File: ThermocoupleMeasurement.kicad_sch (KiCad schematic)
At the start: 11 parts, among them U10 MAX4238ASA, U15 LT1025CN8-PBF, U9 LT1054

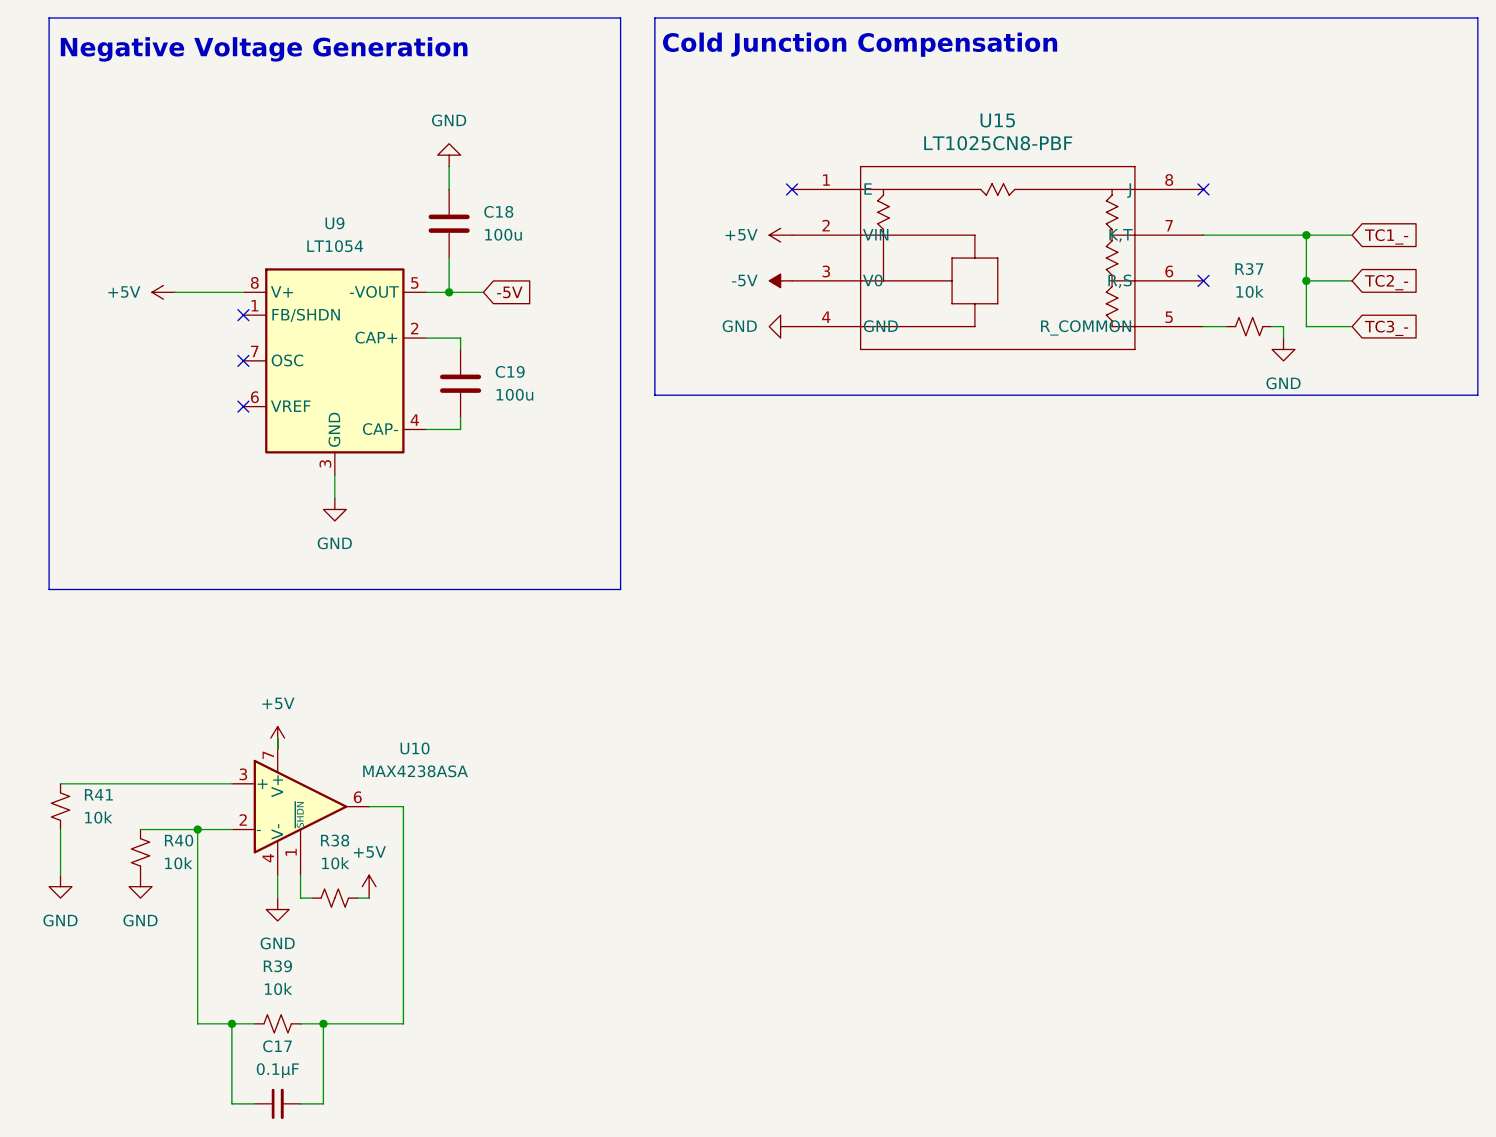
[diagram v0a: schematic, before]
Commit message: add thermocouple filtering, add 5th ADC
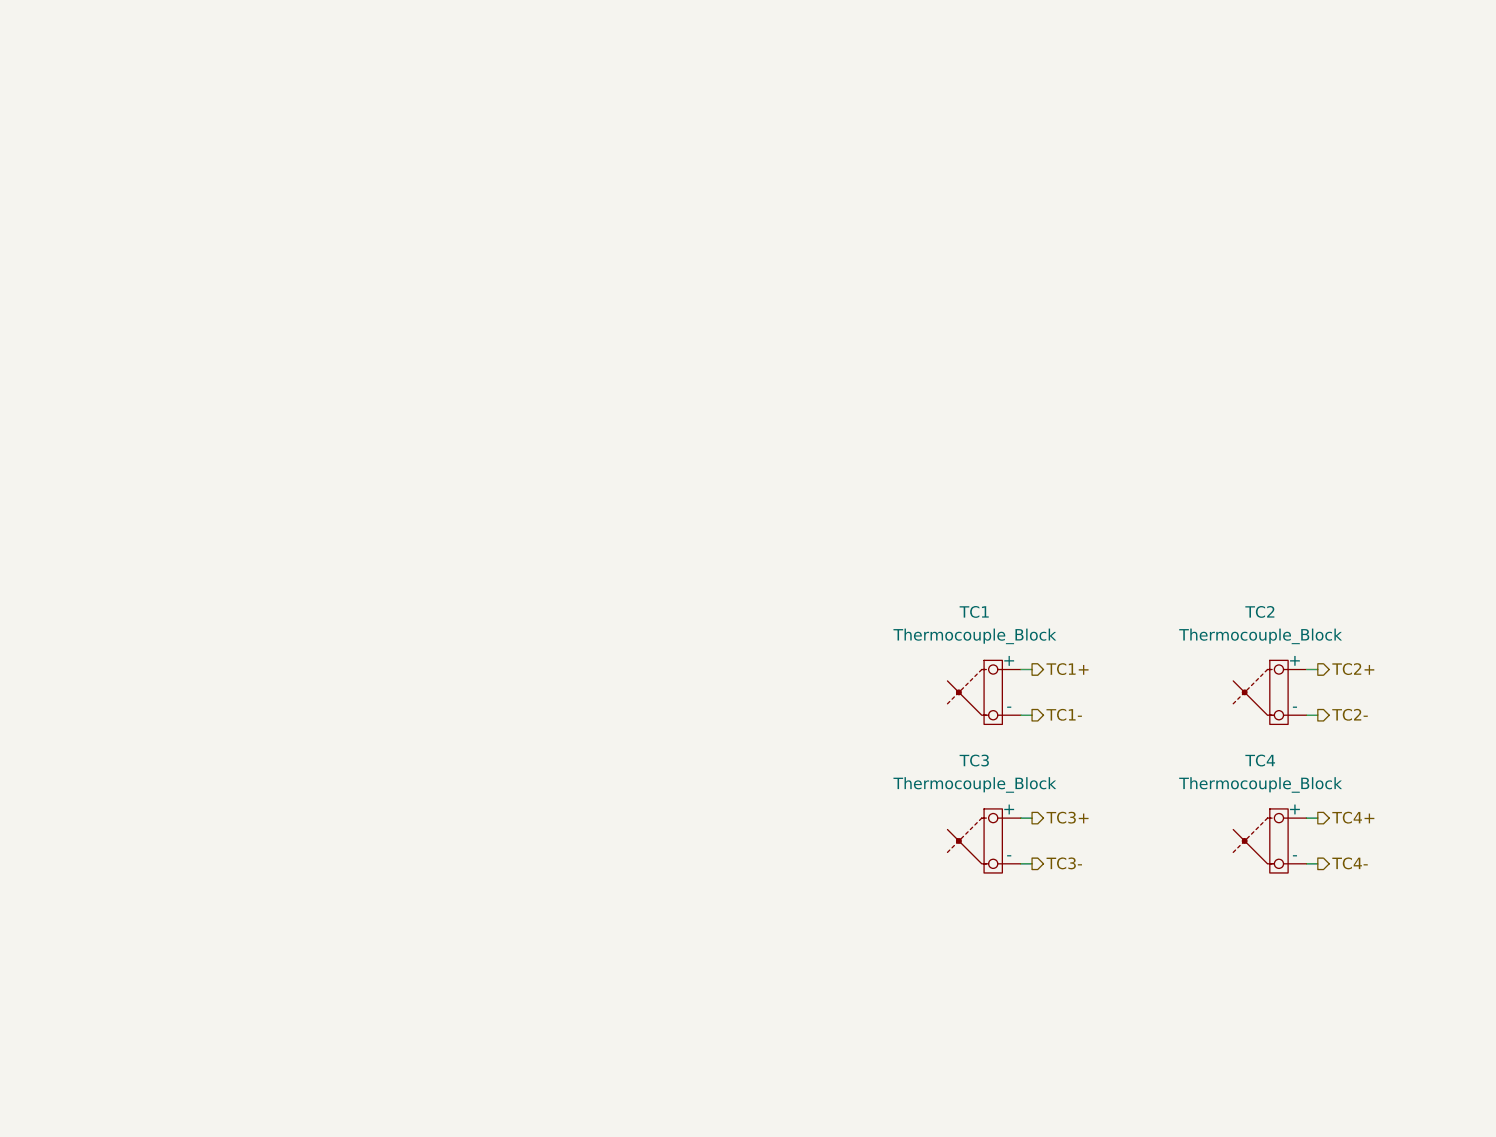
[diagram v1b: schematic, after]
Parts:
- removed C17: 0.1μF, Capacitor_SMD:C_0402_1005Metric, symbol Device:C_Small
- removed C18, C19: 100u, Capacitor_SMD:C_Elec_6.3x5.4, symbol Device:C
- removed R37, R38, R39, R40, R41: 10k, Resistor_SMD:R_0402_1005Metric, symbol Device:R_Small_US
- removed U10: MAX4238ASA, Package_SO:SOIC-8_3.9x4.9mm_P1.27mm, symbol Amplifier_Operational:MAX4238ASA
- removed U15: LT1025CN8-PBF, Footprints:PDIP8_LT1025CN8-PBF_ADI, symbol 2025-02-03_00-05-09:LT1025CN8-PBF
- removed U9: LT1054, Package_SO:SOIC-8_3.9x4.9mm_P1.27mm, symbol Regulator_SwitchedCapacitor:LT1054
- added TC1, TC2, TC3, TC4: Thermocouple_Block, symbol Device:Thermocouple_Block
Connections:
- new net TC1+: TC1.1 (+)
- new net TC1-: TC1.2 (-)
- new net TC2+: TC2.1 (+)
- new net TC2-: TC2.2 (-)
- new net TC3+: TC3.1 (+)
- new net TC3-: TC3.2 (-)
- new net TC4+: TC4.1 (+)
- new net TC4-: TC4.2 (-)
- no-connect marks 6 -> 0
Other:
- note removed: "Cold Junction Compensation"
- note removed: "Negative Voltage Generation"
- company: Queen's Rocket Engineering Team -> (none)
- title: Thermocouple Measurement -> (none)

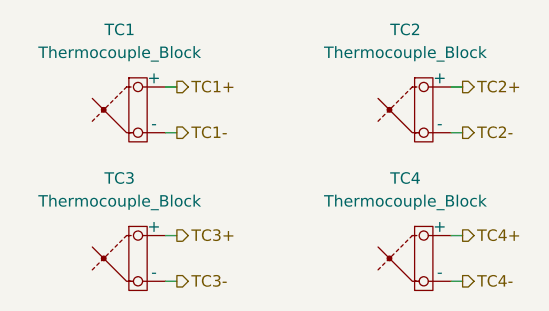
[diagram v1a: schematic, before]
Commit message: add 2 stage lockout to ignitor, add ignitor resistance reading with adc current source
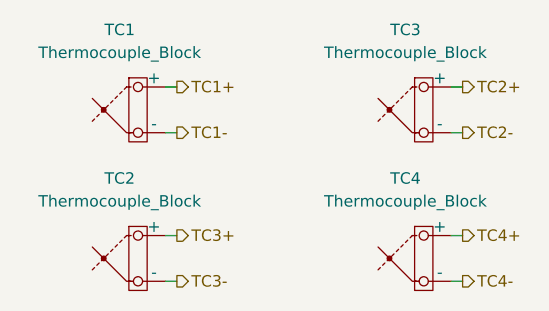
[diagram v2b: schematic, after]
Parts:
- renumbered TC3 to TC2, TC2 to TC3
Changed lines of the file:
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@@
 		(dnp no)
 		(fields_autoplaced yes)
-		(property "Reference" "TC2"
+		(property "Reference" "TC3"
 			(at 156.21 83.82 0)
 			(effects
@@
 			(project "panda"
 				(path "/226c5870-4123-4efa-a2b3-b42d02f59bb7/db011d14-1149-4a3d-969c-b91162637961"
-					(reference "TC2")
+					(reference "TC3")
 					(unit 1)
 				)
@@
 		(dnp no)
 		(fields_autoplaced yes)
-		(property "Reference" "TC3"
+		(property "Reference" "TC2"
 			(at 124.46 100.33 0)
 			(effects
@@
 			(project "panda"
 				(path "/226c5870-4123-4efa-a2b3-b42d02f59bb7/db011d14-1149-4a3d-969c-b91162637961"
-					(reference "TC3")
+					(reference "TC2")
 					(unit 1)
 				)

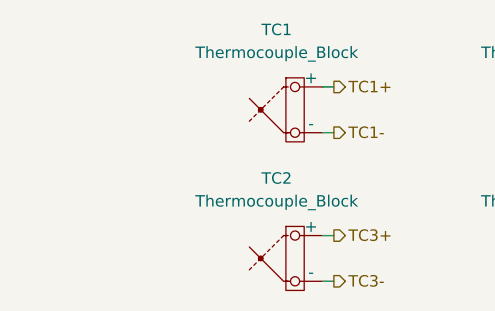
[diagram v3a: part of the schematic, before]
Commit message: change connectors and more progress on pcb
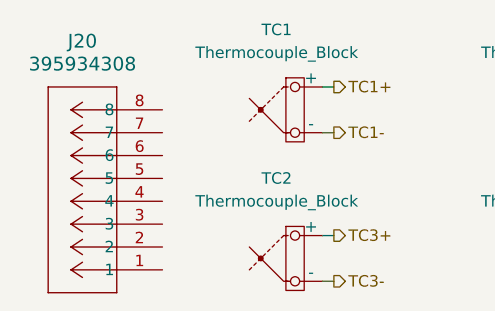
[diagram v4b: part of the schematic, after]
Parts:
- added J20: 395934308, Library:CONN_SD-39543-002_NONE_08P_MOL, symbol 2025-11-28_00-28-49:395934308
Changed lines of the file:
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@@
+	)
+	(symbol
+		(lib_id "2025-11-28_00-28-49:395934308")
+		(at 111.76 110.49 180)
+		(unit 1)
+		(exclude_from_sim no)
+		(in_bom yes)
+		(on_board yes)
+		(dnp no)
+		(fields_autoplaced yes)
+		(property "Reference" "J20"
+			(at 102.87 85.09 0)
+			(effects
+				(font
+					(size 1.524 1.524)
+				)
+			)
+		)
+		(property "Value" "395934308"
+			(at 102.87 87.63 0)
+			(effects
+				(font
+					(size 1.524 1.524)
+				)
+			)
+		)
+		(property "Footprint" "Library:CONN_SD-39543-002_NONE_08P_MOL"
+			(at 111.76 110.49 0)
+			(effects
+				(font
+					(size 1.27 1.27)
+					(italic yes)
+				)
+				(hide yes)
+			)
+		)
+		(property "Datasheet" "https://www.molex.com/en-us/products/part-detail-pdf/395934308?display=pdf"
+			(at 111.76 110.49 0)
+			(effects
+				(font
+					(size 1.27 1.27)
+					(italic yes)
+				)
+				(hide yes)
+			)
+		)
+		(property "Description" ""
+			(at 111.76 110.49 0)
+			(effects
+				(font
+					(size 1.27 1.27)
+				)
+				(hide yes)
+			)
+		)
+		(pin "1"
+		)
+		(pin "5"
+		)
+		(pin "2"
+		)
+		(pin "3"
+		)
+		(pin "8"
+		)
+		(pin "4"
+		)
+		(pin "6"
+		)
+		(pin "7"
+		)
+		(instances
+			(project ""
+				(path "/226c5870-4123-4efa-a2b3-b42d02f59bb7/db011d14-1149-4a3d-969c-b91162637961"
+					(reference "J20")
+					(unit 1)
+				)
+			)
+		)
 	)
 	(symbol

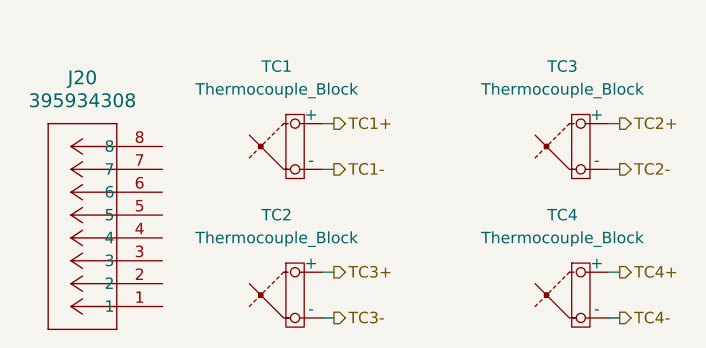
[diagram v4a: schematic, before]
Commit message: change clamping resistors on tc adcs for lower leakage current
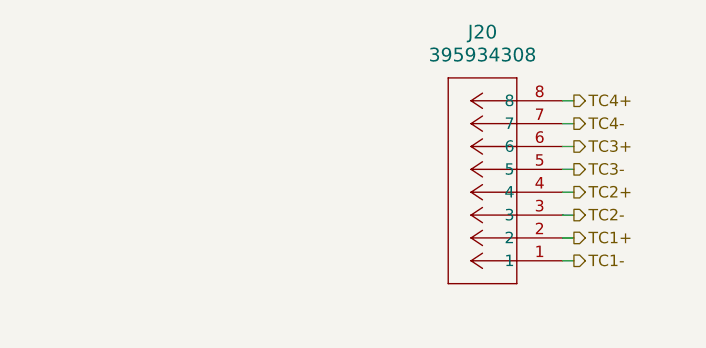
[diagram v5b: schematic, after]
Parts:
- removed TC1, TC2, TC3, TC4: Thermocouple_Block, symbol Device:Thermocouple_Block
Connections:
- net TC1+: now also J20.2
- net TC1-: now also J20.1
- net TC2+: now also J20.4
- net TC2-: now also J20.3
- net TC3+: now also J20.6
- net TC3-: now also J20.5
- net TC4+: now also J20.8
- net TC4-: now also J20.7
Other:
- moved on the sheet: J20

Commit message: Update version number in KiCad files
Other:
- company: (none) -> Queen's Rocket Engineering Team
- title: (none) -> PANDA
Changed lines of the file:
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@@
 	(generator_version "9.0")
 	(paper "A4")
+	(title_block
+		(title "PANDA")
+		(date "2025-12-21")
+		(rev "3.0.0")
+		(company "Queen's Rocket Engineering Team")
+	)
 	(wire
 		(pts
